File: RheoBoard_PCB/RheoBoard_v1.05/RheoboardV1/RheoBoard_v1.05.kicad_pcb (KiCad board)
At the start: 2 copper layers, 109 x 126.4 mm, 165 parts, among them J1 JST SH 4-pin 1.00mm, J12 JST SH 4-pin 1.00mm, J17 JST SH 4-pin 1.00mm, J2 PJ-082BH, J3 JST EH 4-pin 2.50mm, J9 JST SH 4-pin 1.00mm, Q10 AO3400A, Q3 AO3400A, Q4 AO3400A, Q8 AO3400A, SW1 TL3301NF160QG/P010515, SW2 TL3301NF160QG/P010515, SW3 TL3301NF160QG/P010515, SW4 TL3301NF160QG/P010515, U1 TPS563203DRLR, U10 JST XH 2-pin 2.50mm, U11 ZR370-02PM / 4.5V / 2.5 LPM /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, U12 TPS259472ARPWR, U13 TCA9517ADGKR, U2 TPS563203DRLR, U3 TPS563203DRLR, U4 TCA9534APWR, U5 MPRLS0025PA00001A, U7 PCA9685PW,118, U8 ZR370-02PM / 4.5V / 2.5 LPM /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, U9 JST XH 2-pin 2.50mm

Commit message: Update RheoBoard design files and documentation
- Renamed schematic and PCB file references for consistency across the project.
- Added a new SOD-123 diode footprint with detailed properties, including a datasheet link and assembly information.
- Adjusted global labels and junctions in the schematic for improved clarity and accuracy.
- Updated image dimensions in documentation for better presentation.

These changes enhance the organization, usability, and clarity of the RheoBoard project files and documentation.
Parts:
- removed D1: B540C-13-F, Diode_SMD:D_SMC
- added D37: BZT52C10-7-F, Diode_SMD:D_SOD-123, F.Cu at (134.8, 52.8)
- added Q11: DMP6023LE-13, Package_TO_SOT_SMD:SOT-223-3_TabPin2, F.Cu at (132.5, 45.0)
- added R85: 10K/0603/1%, Resistor_SMD:R_0603_1608Metric_Pad0.98x0.95mm_HandSolder, F.Cu at (130.2, 52.8)

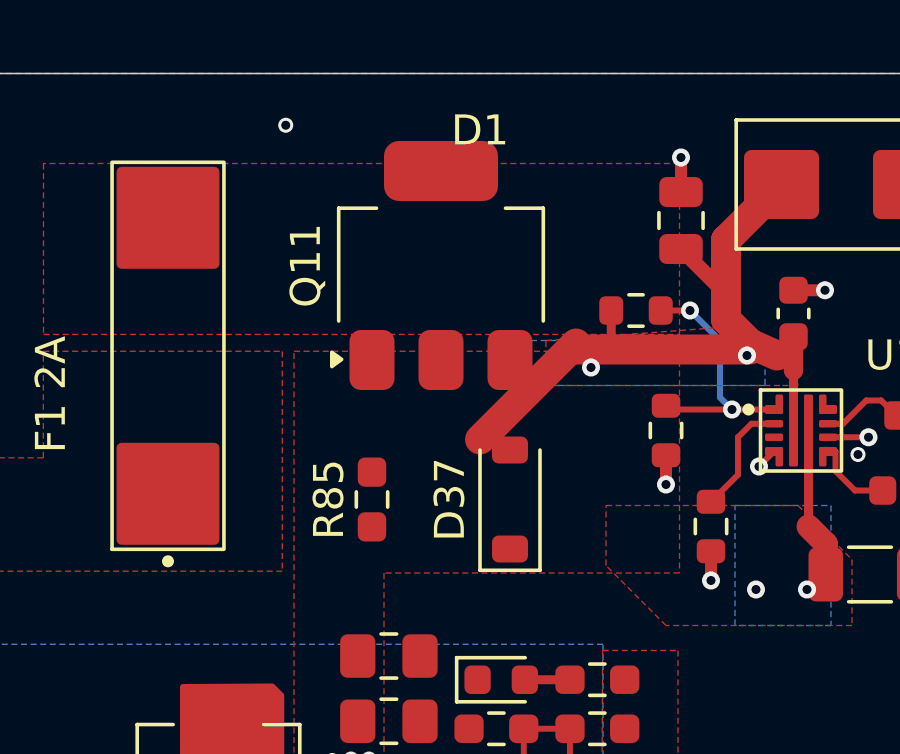
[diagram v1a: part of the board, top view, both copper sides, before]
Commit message: Update RheoBoard PCB and schematic files for improved component alignment and clarity
- Adjusted the orientation and positioning of various properties for the SOD-123 diode footprint in the PCB file to ensure proper alignment.
- Added a new junction in the schematic and modified wire connections for better clarity and accuracy.
- Updated global labels to reflect changes in net names and improved layout consistency.

These changes enhance the usability and accuracy of the RheoBoard design files.
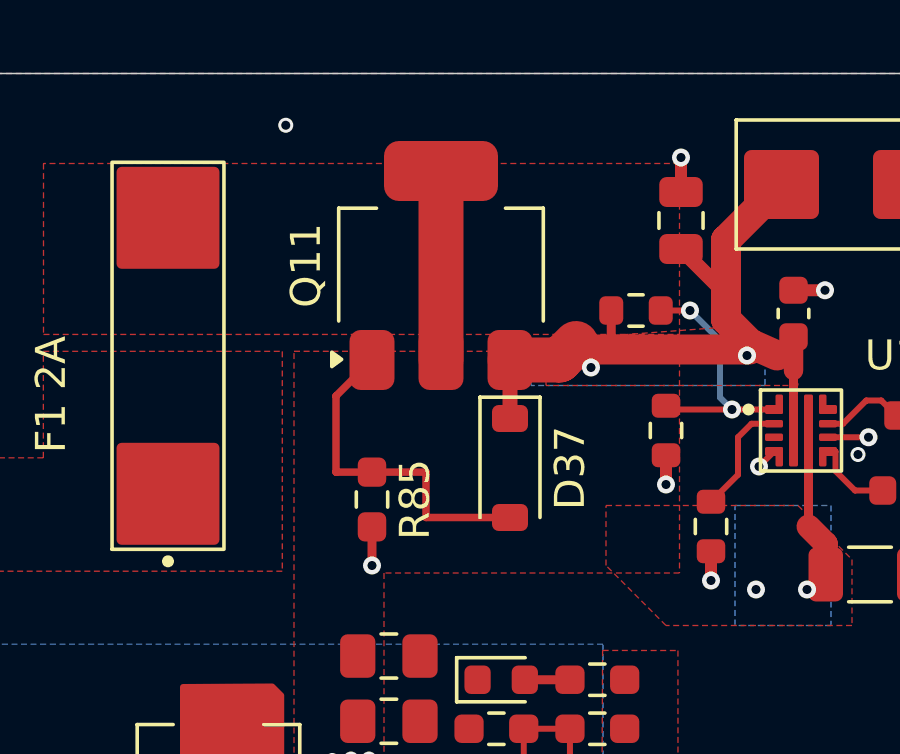
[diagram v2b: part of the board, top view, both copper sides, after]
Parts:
- moved D37 1.05 mm to (134.8, 51.8), turned to -90 degrees
- turned R85 to -90 degrees
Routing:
- net Net-(D37-A): track 0.00 -> 11.5 mm
- net Net-(D1-A): track 0.00 -> 6.30 mm
- net GND: track 16.6 -> 17.8 mm, vias 218 -> 219
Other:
- board text removed: "D1"

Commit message: Update documentation and design files for RheoBoard project
- Revised README.md to enhance clarity on build instructions and component descriptions for RheoBoardOTS - DIY and RheoBoard_v1 - PCB.
- Updated hardware documentation to include detailed specifications for the Cysljoyful AC/DC adapter and its role in the system.
- Enhanced image references and descriptions to align with the latest design changes, including the addition of new images for the power adapter.
- Adjusted schematic and PCB files to improve component alignment and clarity, including the addition of new wire connections and labels.

These updates improve the organization, usability, and clarity of the RheoBoard project documentation and design files.
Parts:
- removed C22: 10nF 50V ±10%, Capacitor_SMD:C_0603_1608Metric_Pad1.08x0.95mm_HandSolder
- removed C47: 100nF 50V X7R ±10%, Capacitor_SMD:C_0603_1608Metric_Pad1.08x0.95mm_HandSolder
- removed R10: 2K2/0603/1%, Resistor_SMD:R_0603_1608Metric_Pad0.98x0.95mm_HandSolder
- removed R11: 4K7/0603/1%, Resistor_SMD:R_0603_1608Metric_Pad0.98x0.95mm_HandSolder
- removed R13, R14: 10K/0603/1%, Resistor_SMD:R_0603_1608Metric_Pad0.98x0.95mm_HandSolder
- removed TP1: TestPoint, TestPoint:TestPoint_Pad_D1.0mm
- removed U4: TCA9534APWR, RheoBoard:TCA9534APWR
- added J19: BUTTONS_GPIO, Connector_PinHeader_2.54mm:PinHeader_1x05_P2.54mm_Vertical, F.Cu at (161.0, 93.5)
- moved R16 71.0 mm to (164.8, 91.0), turned to 180 degrees
- moved R17 70.4 mm to (164.8, 88.5), turned to 180 degrees
- moved R18 59.4 mm to (164.8, 85.9), turned to 180 degrees
- moved R19 57.0 mm to (164.8, 83.4), turned to 180 degrees
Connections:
- R16 pad 1: +3V3 -> /HOST_3V3
- R17 pad 1: +3V3 -> /HOST_3V3
- R18 pad 1: +3V3 -> /HOST_3V3
- R19 pad 1: +3V3 -> /HOST_3V3
- U7 pad 11: unconnected-(U7-PWM5-Pad11) -> VALVE1
- U7 pad 12: unconnected-(U7-PWM6-Pad12) -> VALVE2
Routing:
- net /HOST_3V3: track 37.0 -> 102.9 mm, vias 2 -> 4
- net +3V3: track 334.9 -> 299.9 mm
- net VALVE2: track 81.2 -> 109.5 mm, vias 2 -> 5
- net VALVE1: track 59.1 -> 84.5 mm, vias 2 -> 5
- net Net-(U4-/INT): track 17.8 -> 0.00 mm
- net Net-(U4-A0): track 10.8 -> 0.00 mm
- net /SCL: track 233.6 -> 224.8 mm
- net VALVE1_IN: track 78.9 -> 71.3 mm
- net VALVE2_IN: track 73.4 -> 66.7 mm
- net PUMP1_IN: track 82.1 -> 76.3 mm
- net /SDA: track 235.8 -> 231.7 mm
- net PUMP2_IN: track 63.1 -> 59.5 mm
- net Net-(U4-P3): track 3.38 -> 0.00 mm
- net Net-(U4-P2): track 3.38 -> 0.00 mm

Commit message: Remove obsolete segments and update via connections in RheoBoard v1.05 PCB design file. This cleanup enhances the clarity and accuracy of the design by eliminating unnecessary components and improving the layout of existing connections.
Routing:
- net /HOST_3V3: track 102.9 -> 56.2 mm
- net VALVE2: track 109.5 -> 77.3 mm
- net VALVE1: track 84.5 -> 55.2 mm, vias 5 -> 4
- net PUMP2_IN: track 59.5 -> 38.0 mm
- net PUMP1_IN: track 76.3 -> 56.2 mm
- net VALVE1_IN: track 71.3 -> 54.8 mm
- net VALVE2_IN: track 66.7 -> 50.5 mm
- net GND: vias 219 -> 220

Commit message: Refine README.md and update PCB design for RheoBoard v1.05
- Enhanced README.md for improved clarity on the RheoBoardOTS - DIY and RheoBoard_v1 - PCB descriptions.
- Adjusted component positioning and properties in the RheoBoard v1.05 PCB design file to ensure proper alignment and consistency.
- Updated resistor footprints and orientation for better soldering and assembly.

These changes enhance the documentation and usability of the RheoBoard project.
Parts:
- moved J19 4.30 mm to (165.0, 92.0)
- moved R19 4.18 mm to (165.0, 79.2)
- moved R16 3.83 mm to (168.4, 89.7)
- moved R17 3.75 mm to (168.4, 87.4)
- moved R18 3.69 mm to (168.4, 85.1)
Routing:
- net /HOST_3V3: track 56.2 -> 93.4 mm, vias 4 -> 3
- net VALVE2: track 77.3 -> 109.2 mm, vias 5 -> 4
- net VALVE1: track 55.2 -> 85.7 mm
- net PUMP2_IN: track 38.0 -> 63.8 mm
- net PUMP1_IN: track 56.2 -> 80.8 mm
- net VALVE1_IN: track 54.8 -> 75.7 mm
- net VALVE2_IN: track 50.5 -> 71.2 mm
- net GND: vias 220 -> 205

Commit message: Update README.md and refine PCB design for RheoBoard v1.05
- Enhanced README.md to clarify certification details and added a link to the Certification wiki page.
- Adjusted component positions in the PCB design for improved alignment and consistency.
- Added new silk screen text labels for components to enhance visibility and identification.

These changes improve the documentation and usability of the RheoBoard project.
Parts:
- moved R16 1.12 mm to (169.0, 90.7)
- moved R17 0.60 mm to (169.0, 87.4)
- moved R18 0.60 mm to (169.0, 85.1)
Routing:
- net /HOST_3V3: track 93.4 -> 99.6 mm, vias 3 -> 6
- net VALVE1_IN: track 75.7 -> 76.7 mm
- net VALVE2_IN: track 71.2 -> 71.8 mm
- net PUMP1_IN: track 80.8 -> 81.4 mm
- net PUMP2_IN: track 63.8 -> 64.3 mm
- net GND: vias 205 -> 204
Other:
- board text added: "BUTTONS"
- board text added: "P1"
- board text added: "P2"
- board text added: "R16"
- board text added: "R17"
- board text added: "R18"
- board text added: "R19"
- board text added: "V1"
- board text added: "V2"
